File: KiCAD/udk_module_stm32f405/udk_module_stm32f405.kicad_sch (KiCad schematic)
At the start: 76 parts, among them J1 5V, J2 USB_C_Receptacle, J3 QWIIC, J4 SPI, J5 TC2030_SWD, J6 CONN, J7 ARGB, U1 AMS1117-3.3, U2 STM32F405RGTx, U3 NC7SZ125M5X, U4 MB85RS64, U5 TS3USB30EDGSR, U6 USB3300-EZK, U7 SN74LVC1G14DBV, Y1 25MHz 20pF SMD3225-4P, Y2 32.768kHz 12.5pF SMD3215-2P, Y3 24MHz

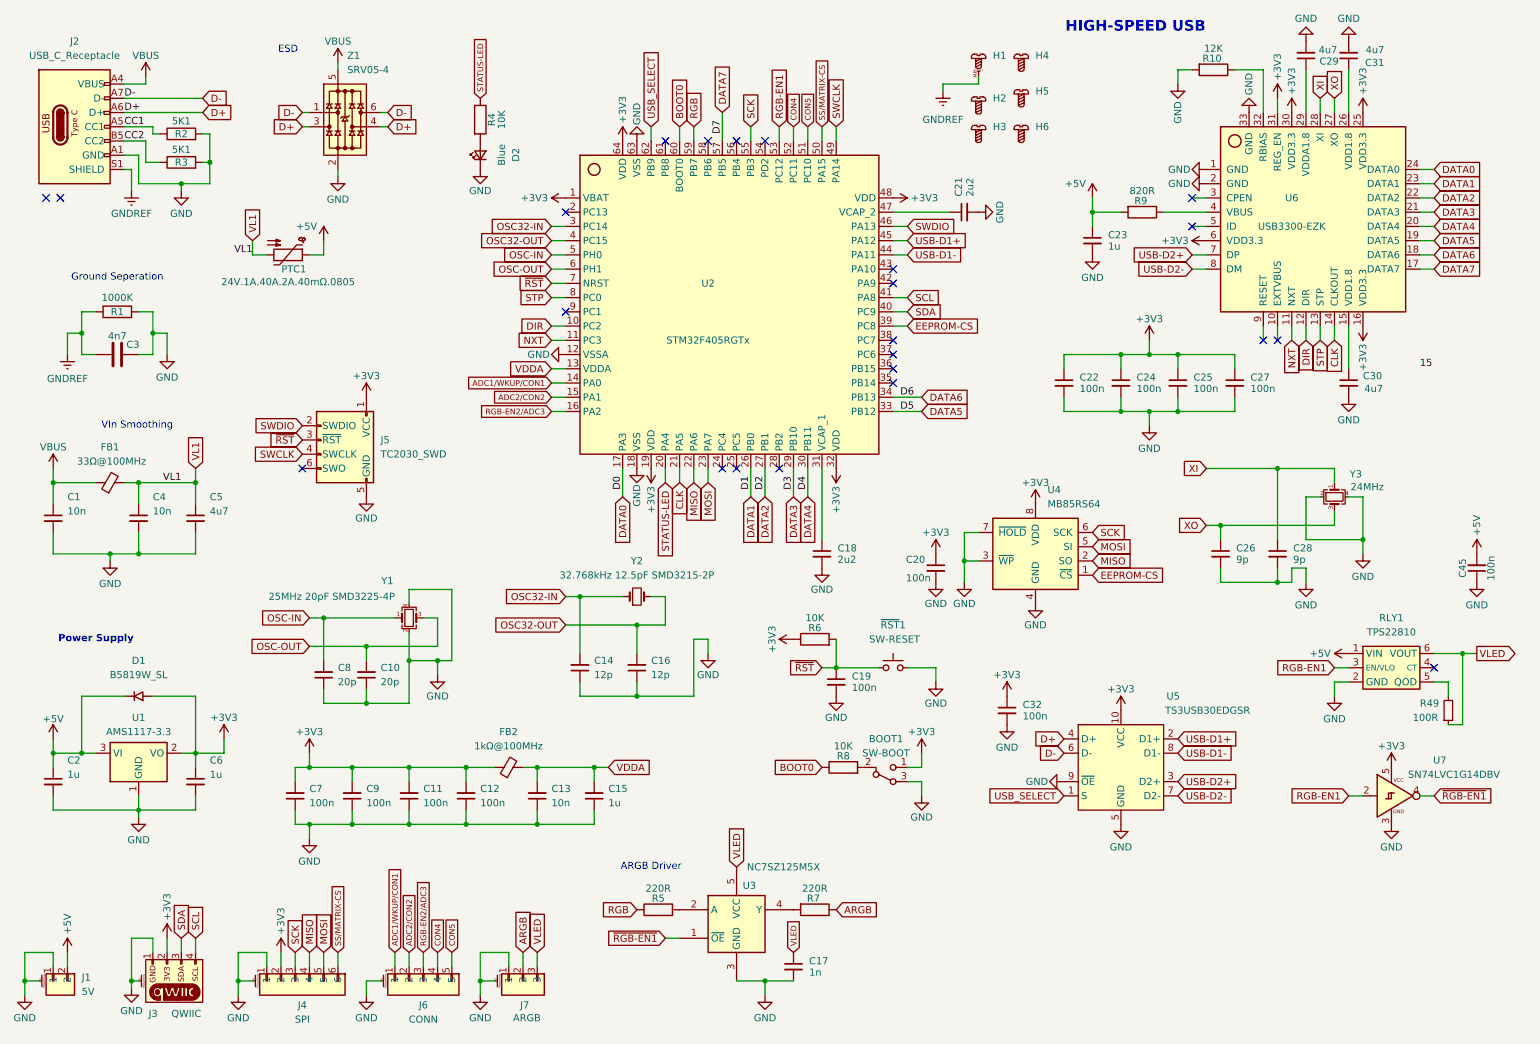
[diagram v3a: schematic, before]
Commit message: move rgb to spi pin
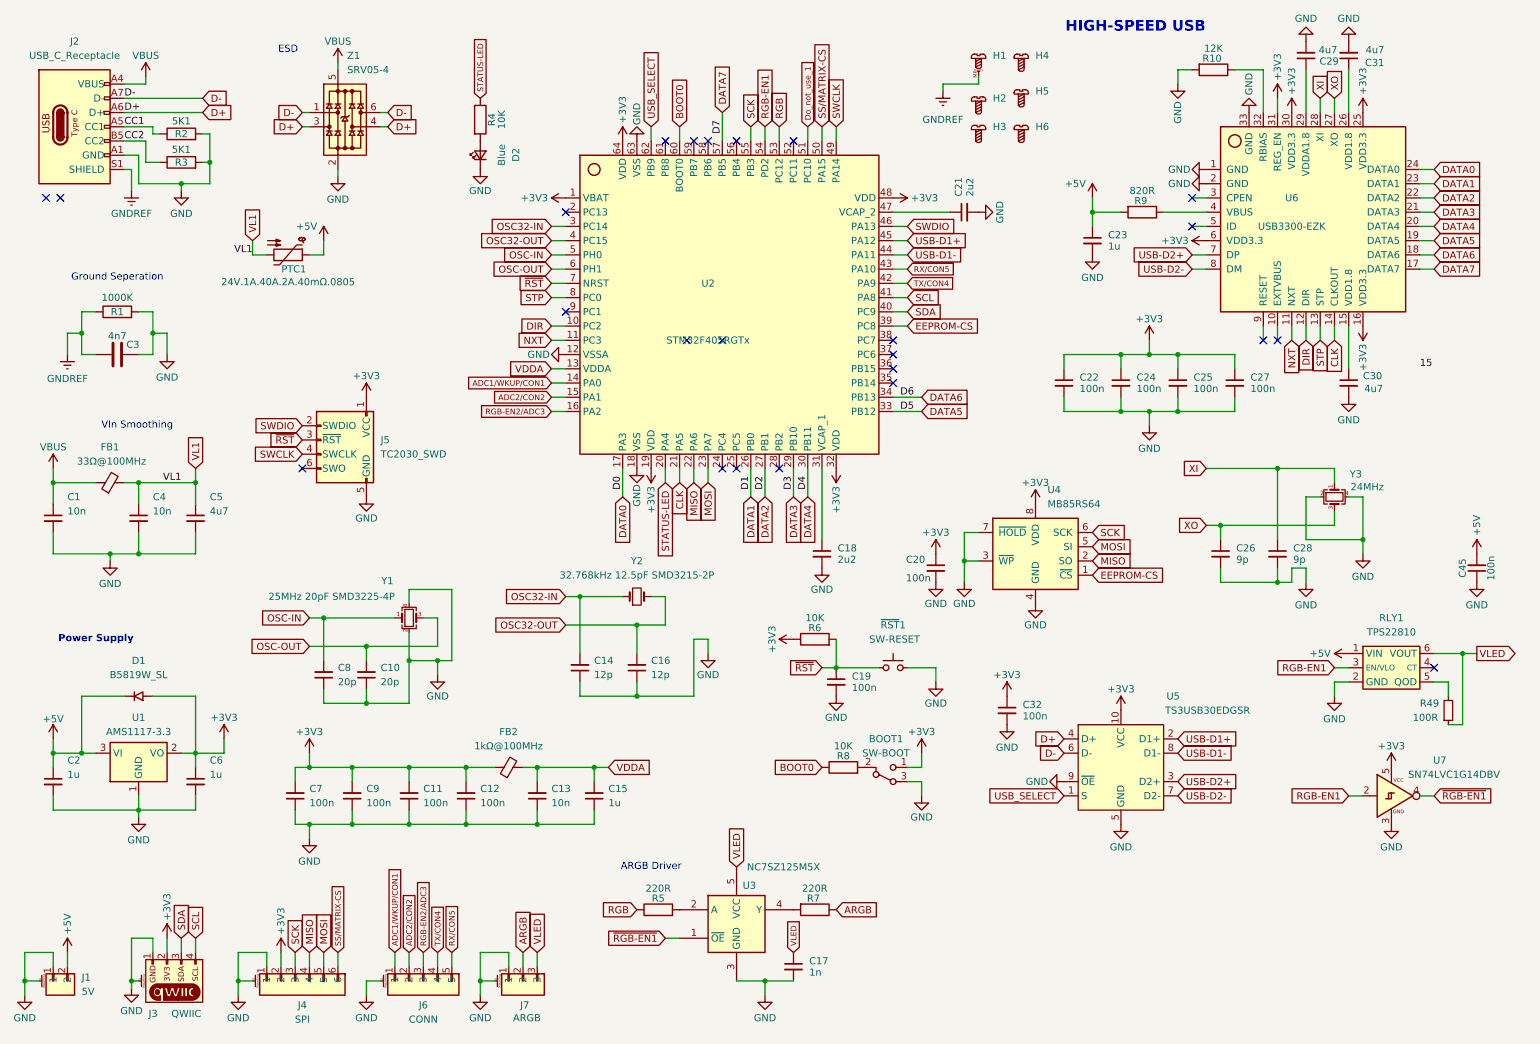
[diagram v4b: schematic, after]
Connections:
- net RGB: now also U2.53 (PC12); no longer U2.59 (PB7)
- net RGB-EN1: now also U2.54 (PD2); no longer U2.53 (PC12)
- net TX/CON4: now reaches U2.42 (PA9)
- net TX/CON4: now also J6.4
- net RX/CON5: now reaches U2.43 (PA10)
- net RX/CON5: now also J6.5
- net CON4: no longer names the net of U2.52 (PC11)
- net CON4: no longer J6.4
- net CON5 renamed Do_not_use_1
- net Do_not_use_1: no longer J6.5
- no-connect marks 23 -> 24
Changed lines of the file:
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@@
 	)
 	(no_connect
+		(at 172.72 76.2)
+	)
+	(no_connect
 		(at 226.06 50.8)
 	)
@@
 	)
 	(no_connect
-		(at 172.72 60.96)
+		(at 142.24 71.12)
 	)
 	(no_connect
@@
 	)
 	(no_connect
-		(at 172.72 71.12)
+		(at 154.94 35.56)
 	)
 	(no_connect
-		(at 172.72 76.2)
-	)
-	(no_connect
-		(at 149.86 35.56)
+		(at 172.72 71.12)
 	)
 	(no_connect
@@
 	)
 	(no_connect
-		(at 67.31 93.98)
+		(at 135.89 71.12)
 	)
 	(no_connect
-		(at 172.72 58.42)
+		(at 137.16 35.56)
+	)
+	(no_connect
+		(at 67.31 93.98)
 	)
 	(wire
@@
 	(wire
 		(pts
+			(xy 149.86 33.02) (xy 149.86 35.56)
+		)
+		(stroke
+			(width 0)
+			(type default)
+		)
+	)
+	(wire
+		(pts
 			(xy 231.14 104.14) (xy 231.14 106.68)
 		)
@@
 	(wire
 		(pts
-			(xy 137.16 33.02) (xy 137.16 35.56)
-		)
-		(stroke
-			(width 0)
-			(type default)
-		)
-	)
-	(wire
-		(pts
 			(xy 73.66 21.59) (xy 73.66 22.86)
 		)
@@
 	(wire
 		(pts
-			(xy 33.02 109.22) (xy 38.1 109.22)
+			(xy 160.02 33.02) (xy 160.02 35.56)
 		)
 		(stroke
@@
 	(wire
 		(pts
-			(xy 48.26 96.52) (xy 38.1 96.52)
+			(xy 33.02 109.22) (xy 38.1 109.22)
 		)
 		(stroke
@@
 	(wire
 		(pts
-			(xy 226.06 50.8) (xy 228.6 50.8)
+			(xy 48.26 96.52) (xy 38.1 96.52)
 		)
 		(stroke
@@
 	(wire
 		(pts
-			(xy 154.94 33.02) (xy 154.94 35.56)
+			(xy 226.06 50.8) (xy 228.6 50.8)
 		)
 		(stroke
@@
 	(wire
 		(pts
-			(xy 157.48 33.02) (xy 157.48 35.56)
+			(xy 17.78 187.96) (xy 17.78 185.42)
 		)
 		(stroke
@@
 	(wire
 		(pts
-			(xy 17.78 187.96) (xy 17.78 185.42)
+			(xy 22.86 180.34) (xy 22.86 182.88)
 		)
 		(stroke
@@
 	(wire
 		(pts
-			(xy 22.86 180.34) (xy 22.86 182.88)
+			(xy 109.22 180.34) (xy 109.22 182.88)
 		)
 		(stroke
@@
 	(wire
 		(pts
-			(xy 109.22 180.34) (xy 109.22 182.88)
+			(xy 17.78 185.42) (xy 20.32 185.42)
 		)
 		(stroke
@@
 	(wire
 		(pts
-			(xy 17.78 185.42) (xy 20.32 185.42)
+			(xy 78.74 133.35) (xy 78.74 135.89)
 		)
 		(stroke
@@
 	(wire
 		(pts
-			(xy 78.74 133.35) (xy 78.74 135.89)
+			(xy 71.12 53.34) (xy 71.12 55.88)
 		)
 		(stroke
@@
 	(wire
 		(pts
-			(xy 71.12 53.34) (xy 71.12 55.88)
+			(xy 152.4 33.02) (xy 152.4 35.56)
 		)
 		(stroke
@@
 	(wire
 		(pts
+			(xy 157.48 33.02) (xy 157.48 35.56)
+		)
+		(stroke
+			(width 0)
+			(type default)
+		)
+	)
+	(wire
+		(pts
 			(xy 88.9 120.65) (xy 91.44 120.65)
 		)
@@
 	(wire
 		(pts
-			(xy 160.02 33.02) (xy 160.02 35.56)
-		)
-		(stroke
-			(width 0)
-			(type default)
-		)
-	)
-	(wire
-		(pts
 			(xy 36.83 186.69) (xy 36.83 185.42)
 		)
@@
 	(wire
 		(pts
-			(xy 152.4 33.02) (xy 152.4 35.56)
+			(xy 139.7 124.46) (xy 137.16 124.46)
 		)
 		(stroke
@@
 	(wire
 		(pts
-			(xy 139.7 124.46) (xy 137.16 124.46)
+			(xy 68.58 120.65) (xy 71.12 120.65)
 		)
 		(stroke
@@
 	(wire
 		(pts
-			(xy 68.58 120.65) (xy 71.12 120.65)
+			(xy 266.7 45.72) (xy 269.24 45.72)
 		)
 		(stroke
@@
 	(wire
 		(pts
-			(xy 266.7 45.72) (xy 269.24 45.72)
+			(xy 172.72 60.96) (xy 175.26 60.96)
+		)
+		(stroke
+			(width 0)
+			(type default)
+		)
+	)
+	(wire
+		(pts
+			(xy 172.72 58.42) (xy 175.26 58.42)
 		)
 		(stroke
@@
 		)
 	)
-	(global_label "RGB"
-		(shape input)
-		(at 137.16 33.02 90)
-		(fields_autoplaced yes)
-		(effects
-			(font
-				(size 1.27 1.27)
-			)
-			(justify left)
-		)
-		(property "Intersheetrefs" "${INTERSHEET_REFS}"
-			(at 137.16 26.2248 90)
-			(effects
-				(font
-					(size 1.27 1.27)
-				)
-				(justify left)
-				(hide yes)
-			)
-		)
-	)
 	(global_label "VDDA"
 		(shape input)
@@
 		)
 	)
+	(global_label "Do_not_use_1"
+		(shape input)
+		(at 157.48 33.02 90)
+		(fields_autoplaced yes)
+		(effects
+			(font
+				(size 1.016 1.016)
+			)
+			(justify left)
+		)
+		(property "Intersheetrefs" "${INTERSHEET_REFS}"
+			(at 157.48 20.3754 90)
+			(effects
+				(font
+					(size 1.27 1.27)
+				)
+				(justify left)
+				(hide yes)
+			)
+		)
+	)
 	(global_label "USB-D1+"
 		(shape input)
@@
 		(effects
 			(font
-				(size 1.016 1.016)
+				(size 1.27 1.27)
 			)
 			(justify left)
 		)
 		(property "Intersheetrefs" "${INTERSHEET_REFS}"
-			(at 160.02 19.1175 90)
+			(at 160.02 15.6415 90)
 			(effects
 				(font
@@
 	(global_label "RGB-EN1"
 		(shape input)
-		(at 152.4 33.02 90)
+		(at 149.86 33.02 90)
 		(fields_autoplaced yes)
 		(effects
@@
 		)
 		(property "Intersheetrefs" "${INTERSHEET_REFS}"
-			(at 152.4 20.9634 90)
+			(at 149.86 20.9634 90)
 			(effects
 				(font
@@
 		)
 	)
-	(global_label "CON4"
+	(global_label "TX{slash}CON4"
 		(shape input)
-		(at 154.94 33.02 90)
+		(at 175.26 60.96 0)
 		(fields_autoplaced yes)
 		(effects
@@
 		)
 		(property "Intersheetrefs" "${INTERSHEET_REFS}"
-			(at 154.94 26.5197 90)
+			(at 184.5664 60.96 0)
 			(effects
 				(font
@@
 		)
 	)
+	(global_label "RGB"
+		(shape input)
+		(at 152.4 33.02 90)
+		(fields_autoplaced yes)
+		(effects
+			(font
+				(size 1.27 1.27)
+			)
+			(justify left)
+		)
+		(property "Intersheetrefs" "${INTERSHEET_REFS}"
+			(at 152.4 26.2248 90)
+			(effects
+				(font
+					(size 1.27 1.27)
+				)
+				(justify left)
+				(hide yes)
+			)
+		)
+	)
 	(global_label "DATA0"
 		(shape input)
@@
 		)
 	)
-	(global_label "CON4"
+	(global_label "TX{slash}CON4"
 		(shape input)
 		(at 91.44 180.34 90)
@@
 		)
 		(property "Intersheetrefs" "${INTERSHEET_REFS}"
-			(at 91.44 173.8397 90)
+			(at 91.44 171.0336 90)
 			(effects
 				(font
@@
 		)
 	)
-	(global_label "CON5"
+	(global_label "RX{slash}CON5"
 		(shape input)
 		(at 93.98 180.34 90)
@@
 		)
 		(property "Intersheetrefs" "${INTERSHEET_REFS}"
-			(at 93.98 173.8397 90)
+			(at 93.98 170.7917 90)
 			(effects
 				(font
@@
 		)
 	)
-	(global_label "CON5"
+	(global_label "RX{slash}CON5"
 		(shape input)
-		(at 157.48 33.02 90)
+		(at 175.26 58.42 0)
 		(fields_autoplaced yes)
 		(effects
@@
 		)
 		(property "Intersheetrefs" "${INTERSHEET_REFS}"
-			(at 157.48 26.5197 90)
+			(at 184.8083 58.42 0)
 			(effects
 				(font
